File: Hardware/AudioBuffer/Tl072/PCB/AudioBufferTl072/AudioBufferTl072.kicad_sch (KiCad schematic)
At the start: 34 parts, among them J1 Conn_01x06_Male, J2 Conn_01x02_Pin, J3 Conn_01x06_Male, J4 Conn_01x02_Pin, J5 AudioJack3, J6 AudioJack3, U1 TL072, U2 TL072

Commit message: Added consistency
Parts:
- J1: footprint Connector_PinSocket_2.54mm:PinSocket_1x06_P2.54mm_Vertical -> Connector_PinHeader_2.54mm:PinHeader_1x06_P2.54mm_Horizontal
- J2: footprint (none) -> Connector_PinHeader_2.54mm:PinHeader_1x02_P2.54mm_Horizontal
- J3: footprint Connector_PinSocket_2.54mm:PinSocket_1x06_P2.54mm_Vertical -> Connector_PinSocket_2.54mm:PinSocket_1x06_P2.54mm_Horizontal
- J4: footprint (none) -> Connector_PinSocket_2.54mm:PinSocket_1x02_P2.54mm_Horizontal
- J5, J6: footprint Protoplasma.pretty:PJ-307 -> Protoplasma:PJ-307
- U1, U2: footprint (none) -> Package_DIP:DIP-8_W7.62mm
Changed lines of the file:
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@@
 			)
 		)
-		(property "Footprint" ""
+		(property "Footprint" "Package_DIP:DIP-8_W7.62mm"
 			(at 115.57 179.07 0)
 			(effects
@@
 			)
 		)
-		(property "Footprint" ""
+		(property "Footprint" "Connector_PinHeader_2.54mm:PinHeader_1x02_P2.54mm_Horizontal"
 			(at 22.86 107.95 0)
 			(effects
@@
 			)
 		)
-		(property "Footprint" ""
+		(property "Footprint" "Package_DIP:DIP-8_W7.62mm"
 			(at 124.46 34.29 0)
 			(effects
@@
 			)
 		)
-		(property "Footprint" ""
+		(property "Footprint" "Package_DIP:DIP-8_W7.62mm"
 			(at 138.43 179.07 0)
 			(effects
@@
 			)
 		)
-		(property "Footprint" "Protoplasma.pretty:PJ-307"
+		(property "Footprint" "Protoplasma:PJ-307"
 			(at 180.34 53.34 0)
 			(effects
@@
 			)
 		)
-		(property "Footprint" "Connector_PinSocket_2.54mm:PinSocket_1x06_P2.54mm_Vertical"
+		(property "Footprint" "Connector_PinSocket_2.54mm:PinSocket_1x06_P2.54mm_Horizontal"
 			(at 231.14 86.36 0)
 			(effects
@@
 			)
 		)
-		(property "Footprint" ""
+		(property "Footprint" "Package_DIP:DIP-8_W7.62mm"
 			(at 124.46 69.85 0)
 			(effects
@@
 			)
 		)
-		(property "Footprint" "Connector_PinSocket_2.54mm:PinSocket_1x06_P2.54mm_Vertical"
+		(property "Footprint" "Connector_PinHeader_2.54mm:PinHeader_1x06_P2.54mm_Horizontal"
 			(at 22.86 82.55 0)
 			(effects
@@
 			)
 		)
-		(property "Footprint" ""
+		(property "Footprint" "Connector_PinSocket_2.54mm:PinSocket_1x02_P2.54mm_Horizontal"
 			(at 231.14 107.95 0)
 			(effects
@@
 			)
 		)
-		(property "Footprint" ""
+		(property "Footprint" "Package_DIP:DIP-8_W7.62mm"
 			(at 88.9 144.78 0)
 			(effects
@@
 			)
 		)
-		(property "Footprint" "Protoplasma.pretty:PJ-307"
+		(property "Footprint" "Protoplasma:PJ-307"
 			(at 180.34 125.73 0)
 			(effects
@@
 			)
 		)
-		(property "Footprint" ""
+		(property "Footprint" "Package_DIP:DIP-8_W7.62mm"
 			(at 88.9 109.22 0)
 			(effects

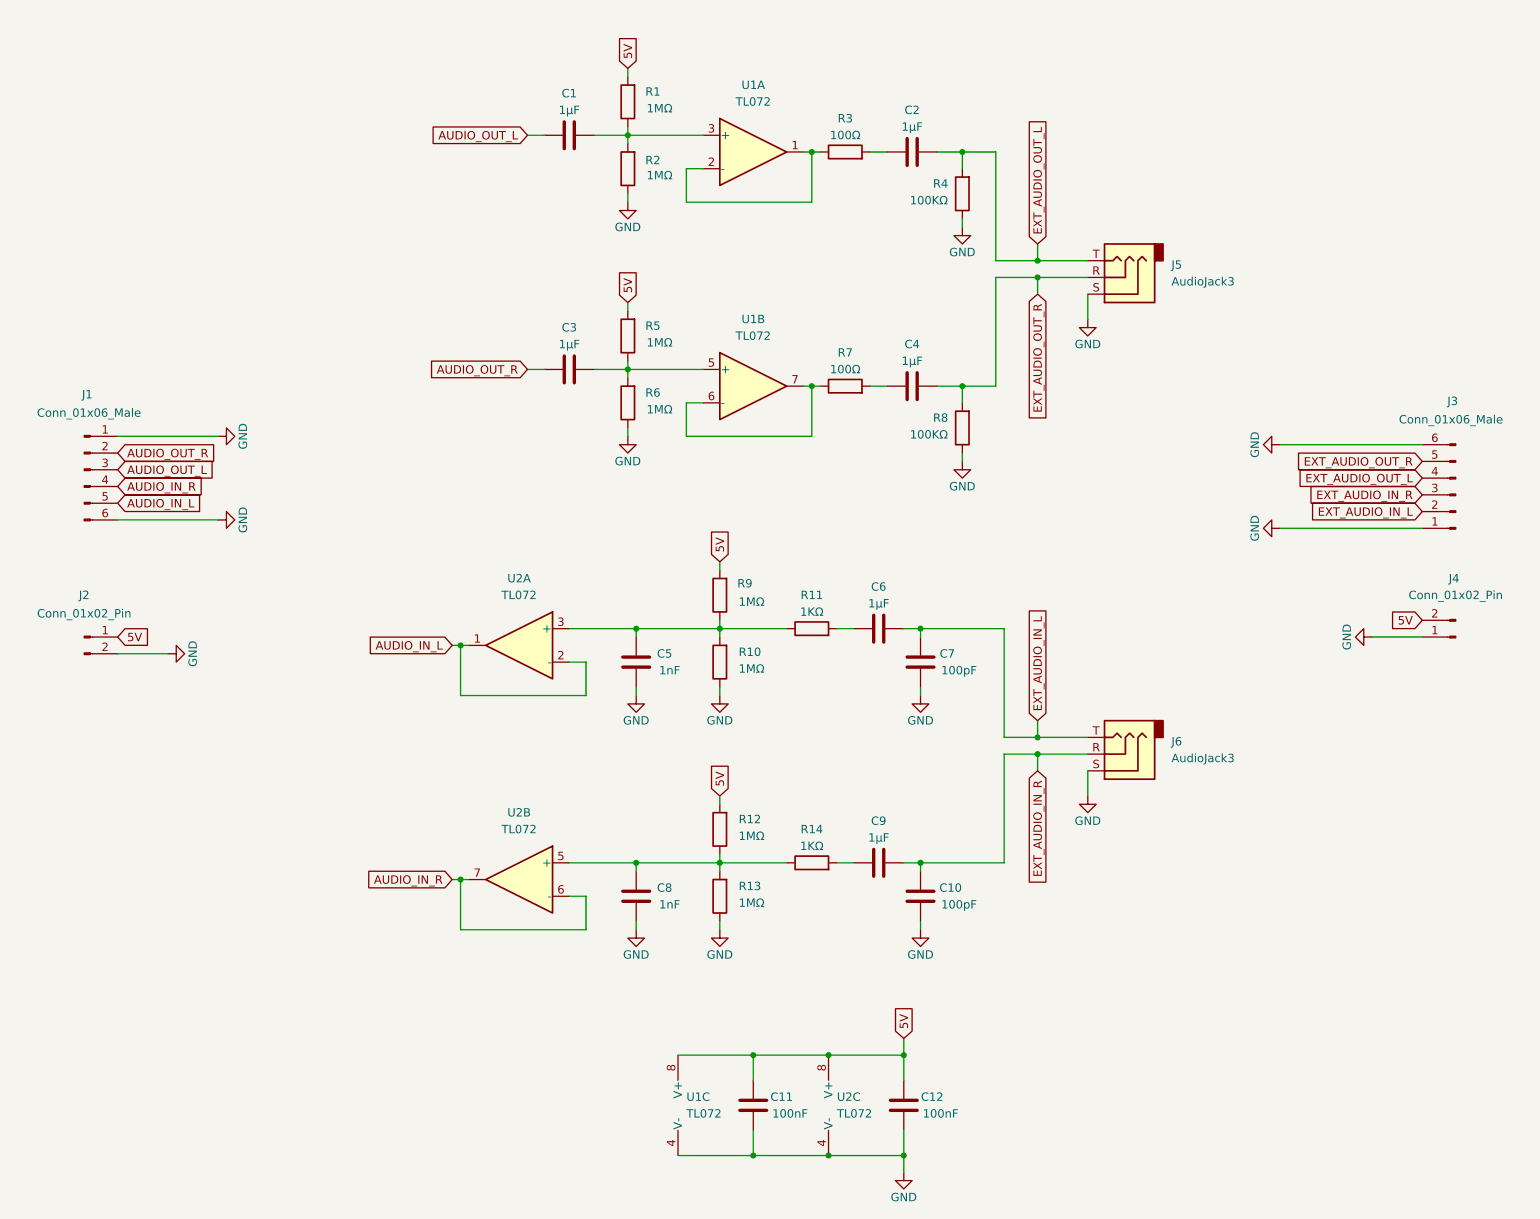
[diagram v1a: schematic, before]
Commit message: Updates to audio buffer
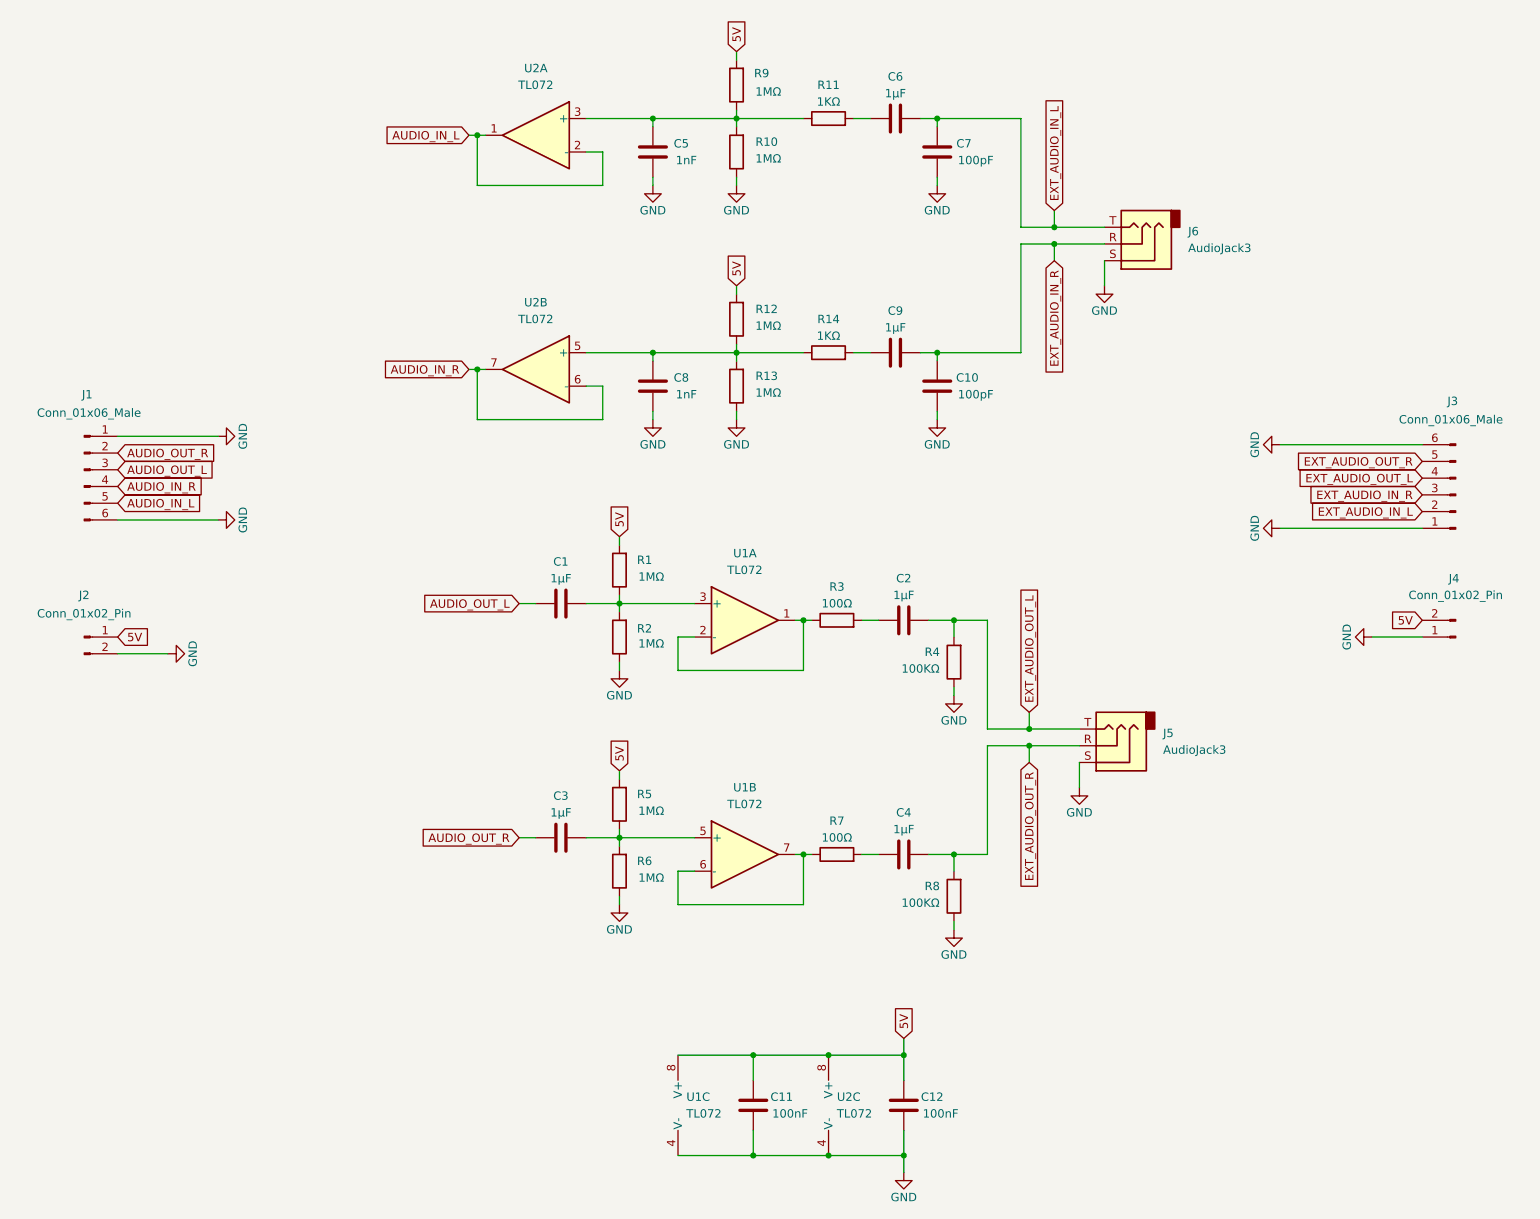
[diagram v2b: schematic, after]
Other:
- moved on the sheet: C1, C10, C2, C3, C4, C5, C6, C7, C8, C9, J5, J6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

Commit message: Isolator added
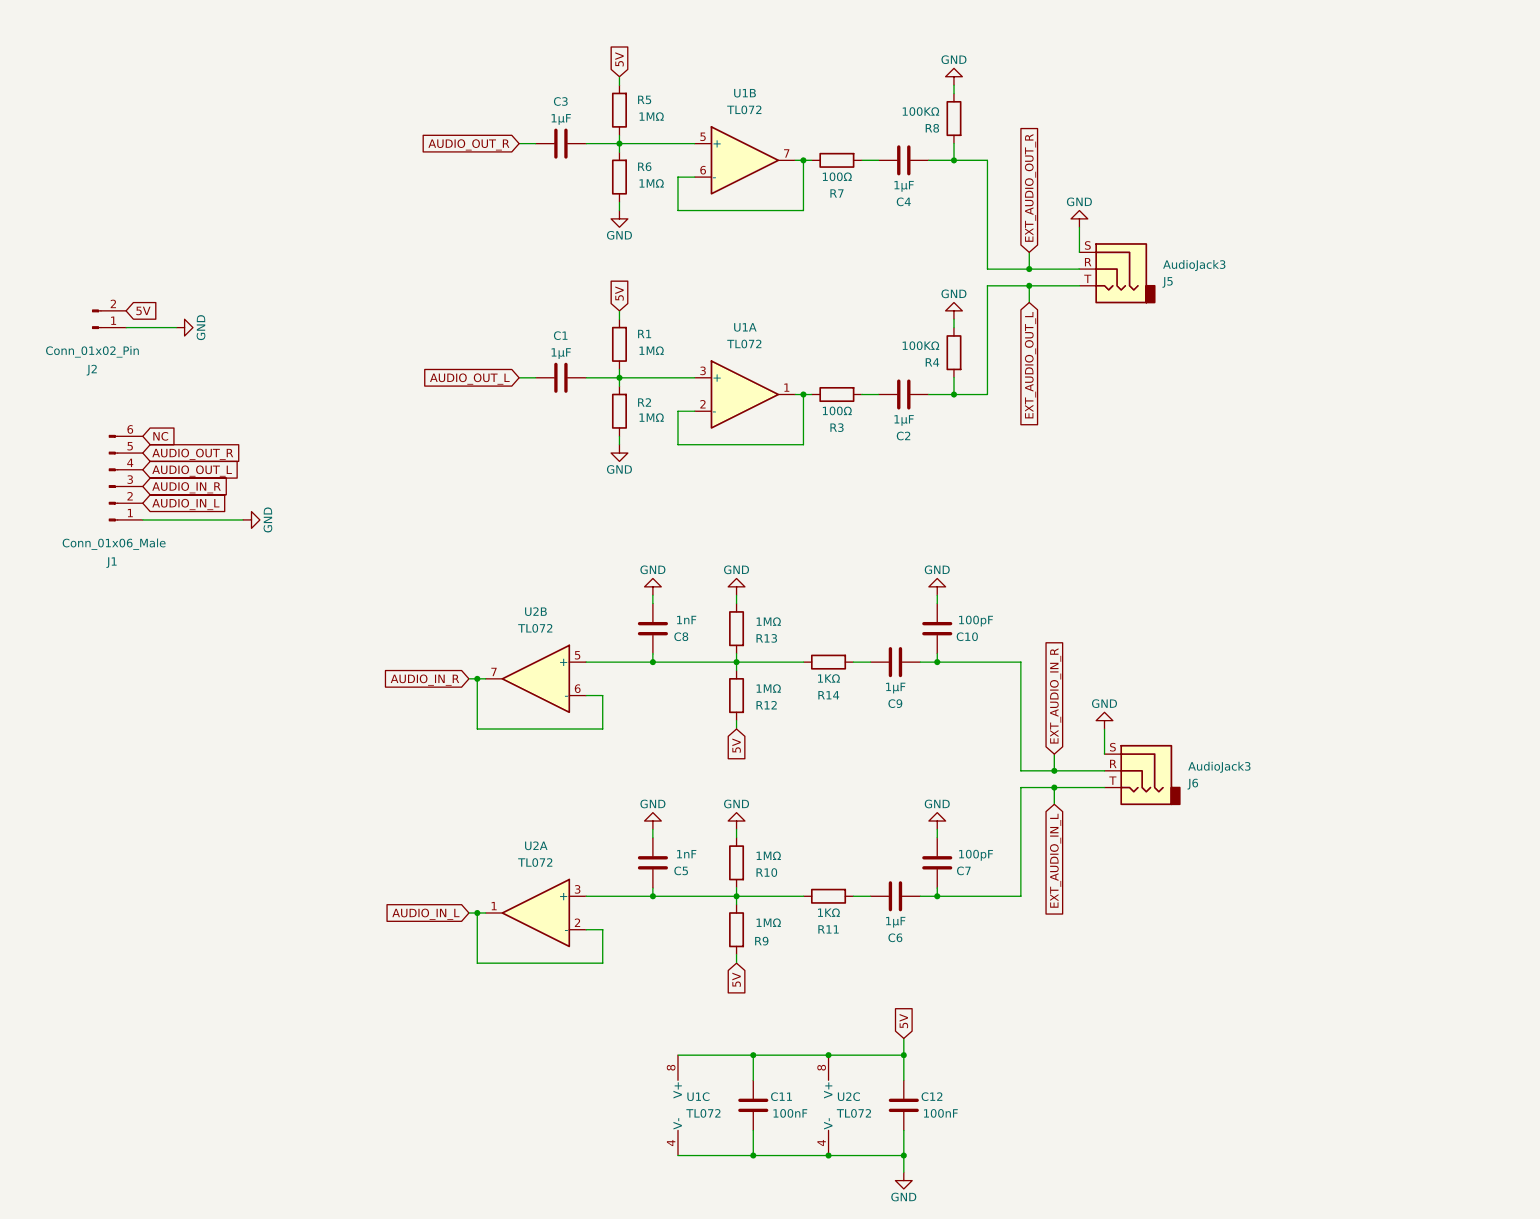
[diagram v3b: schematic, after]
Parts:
- removed J3: Conn_01x06_Male, Connector_PinSocket_2.54mm:PinSocket_1x06_P2.54mm_Horizontal, symbol Connector:Conn_01x06_Male
- removed J4: Conn_01x02_Pin, Connector_PinSocket_2.54mm:PinSocket_1x02_P2.54mm_Horizontal, symbol Connector:Conn_01x02_Pin
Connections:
- net 5V: now also J2.2 (Pin_2); no longer J2.1 (Pin_1)
- net AUDIO_IN_L: now also J1.2 (Pin_2); no longer J1.5 (Pin_5)
- net AUDIO_IN_R: now also J1.3 (Pin_3); no longer J1.4 (Pin_4)
- net AUDIO_OUT_L: now also J1.4 (Pin_4); no longer J1.3 (Pin_3)
- net AUDIO_OUT_R: now also J1.5 (Pin_5); no longer J1.2 (Pin_2)
- net GND: now also J2.1 (Pin_1); no longer J1.6 (Pin_6), J2.2 (Pin_2)
- new net NC: J1.6 (Pin_6)
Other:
- moved on the sheet: C1, C10, C2, C3, C4, C5, C6, C7, C8, C9, J1, J2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
